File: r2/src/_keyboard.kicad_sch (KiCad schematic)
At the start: 38 parts, among them SW1 8HG-P-A-S1-03-065, SW10 8HG-P-A-S1-03-065, SW11 8HG-P-A-S1-03-065, SW12 8HG-P-A-S1-03-065, SW13 8HG-P-A-S1-03-065, SW14 8HG-P-A-S1-03-065, SW15 8HG-P-A-S1-03-065, SW16 8HG-P-A-S1-03-065, SW17 8HG-P-A-S1-03-065, SW18 8HG-P-A-S1-03-065, SW19 8HG-P-A-S1-03-065, SW2 8HG-P-A-S1-03-065, SW20 8HG-P-A-S1-03-065, SW21 8HG-P-A-S1-03-065, SW22 8HG-P-A-S1-03-065, SW23 8HG-P-A-S1-03-065, SW24 8HG-P-A-S1-03-065, SW25 8HG-P-A-S1-03-065, SW26 8HG-P-A-S1-03-065, SW27 8HG-P-A-S1-03-065, SW28 8HG-P-A-S1-03-065, SW29 8HG-P-A-S1-03-065, SW3 8HG-P-A-S1-03-065, SW30 8HG-P-A-S1-03-065, SW31 8HG-P-A-S1-03-065, SW32 8HG-P-A-S1-03-065, SW33 8HG-P-A-S1-03-065, SW34 8HG-P-A-S1-03-065, SW4 8HG-P-A-S1-03-065, SW5 8HG-P-A-S1-03-065, SW6 8HG-P-A-S1-03-065, SW7 8HG-P-A-S1-03-065, SW8 8HG-P-A-S1-03-065, SW9 8HG-P-A-S1-03-065, U7 PCA9555PW, U8 PCA9555PW

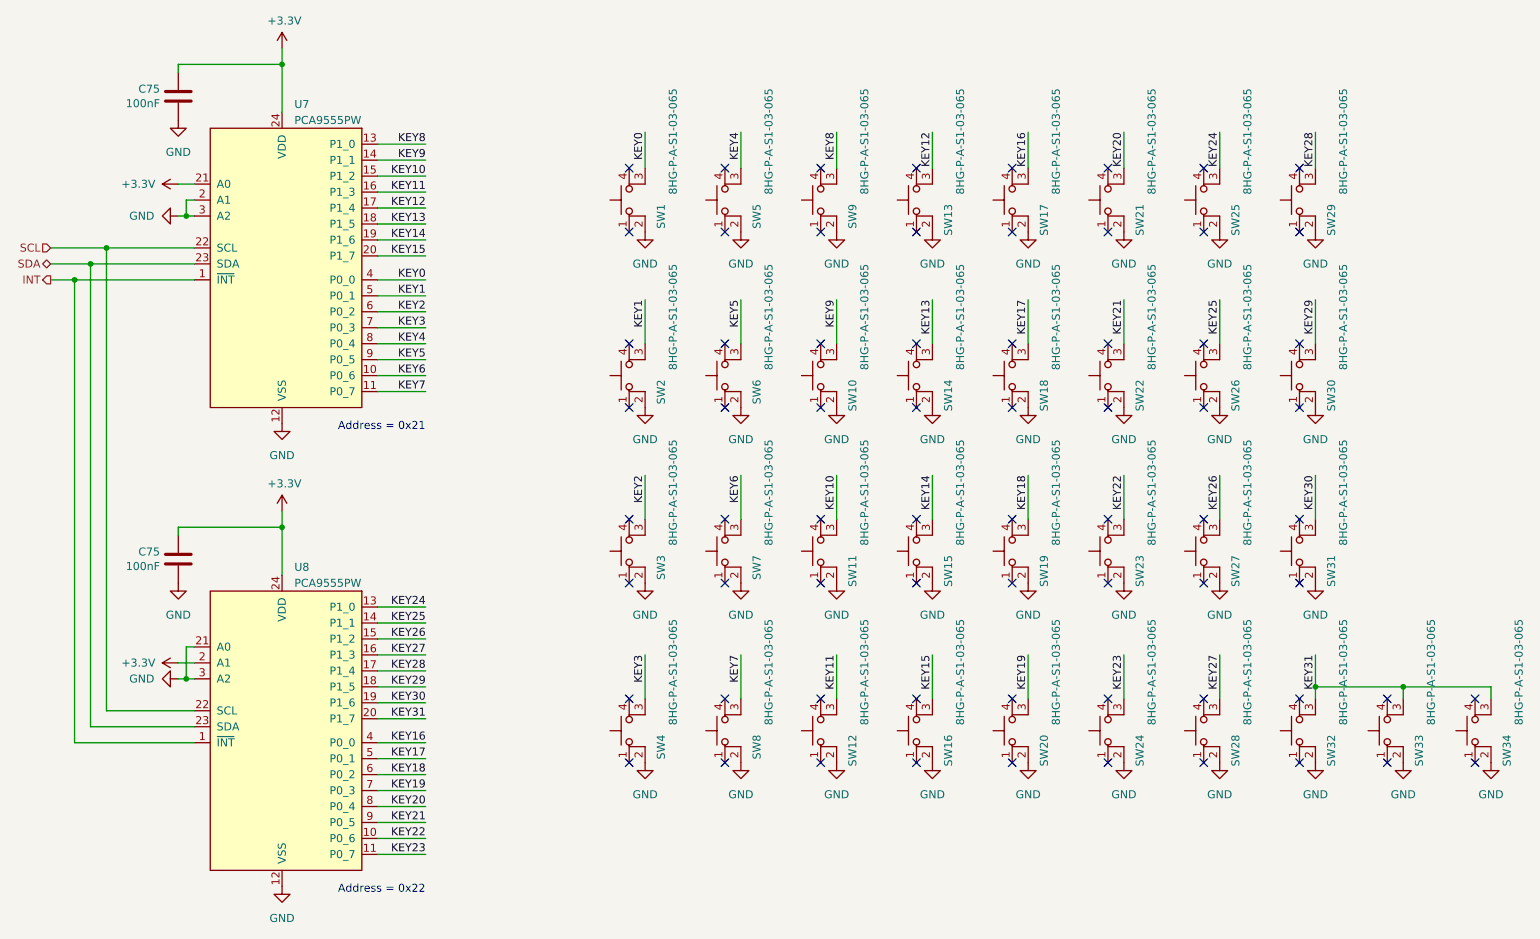
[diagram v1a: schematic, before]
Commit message: Fix off-grid ERC errors so whole schematic is on 1.27mm grid
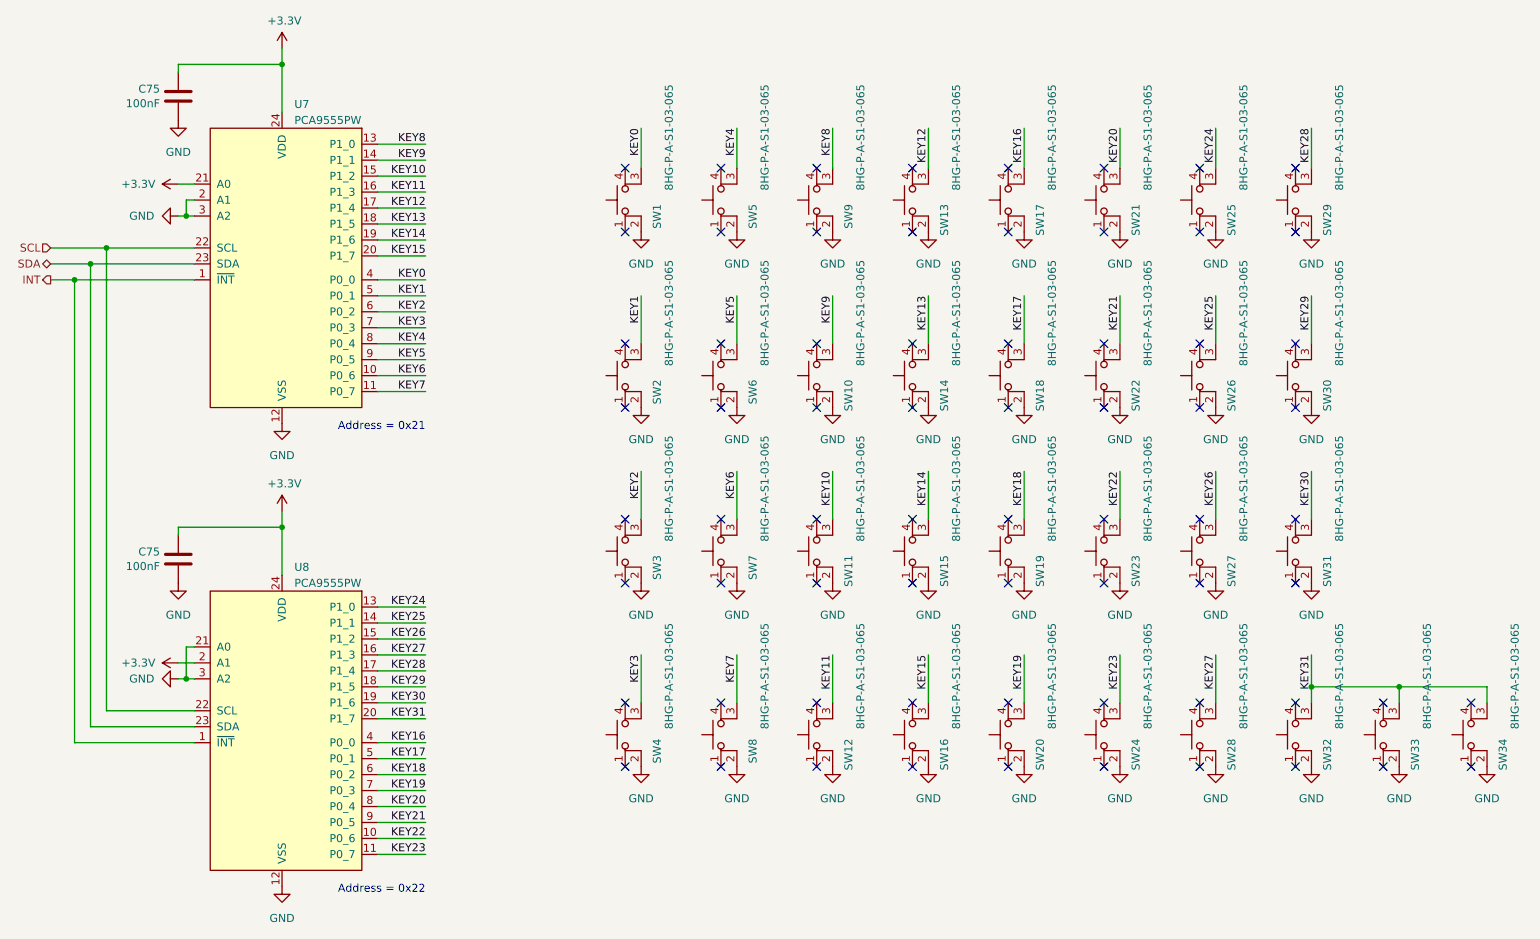
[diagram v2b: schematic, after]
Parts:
- SW1, SW10, SW11, SW12, SW13, SW14, SW15, SW16, SW17, SW18, SW19, SW2, SW20, SW21, SW22, SW23, SW24, SW25, SW26, SW27, SW28, SW29, SW3, SW30, SW31, SW32, SW33, SW34, SW4, SW5, SW6, SW7, SW8, SW9: footprint jeffmakes-footprints:SW_SPST_TACT_6x6_REV_MOUNT -> jeffmakes-footprints:SW_SPST_TACT_6x6_REV_MOUNT_ALT1
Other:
- moved on the sheet: SW1, SW10, SW11, SW12, SW13, SW14, SW15, SW16, SW17, SW18, SW19, SW2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

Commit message: Set title block contents
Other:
- company: (none) -> Monad Gottfried Ltd. 2023
- title: (none) -> Troopers 23 Badge
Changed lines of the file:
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@@
 (kicad_sch (version 20230409) (generator eeschema)
   (paper "A4")
+  (title_block
+    (title "Troopers 23 Badge")
+    (rev "r2")
+    (company "Monad Gottfried Ltd. 2023")
+    (comment 1 "for ERNW Enno Rey Netzwerke GmbH")
+  )
   (junction (at 44.45 60.96) (diameter 0) (color 0 0 0 0)
   )
